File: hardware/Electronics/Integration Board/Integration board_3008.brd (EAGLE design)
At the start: 66.3 x 58.3 mm, 11 parts, among them J3 CONN_20X2

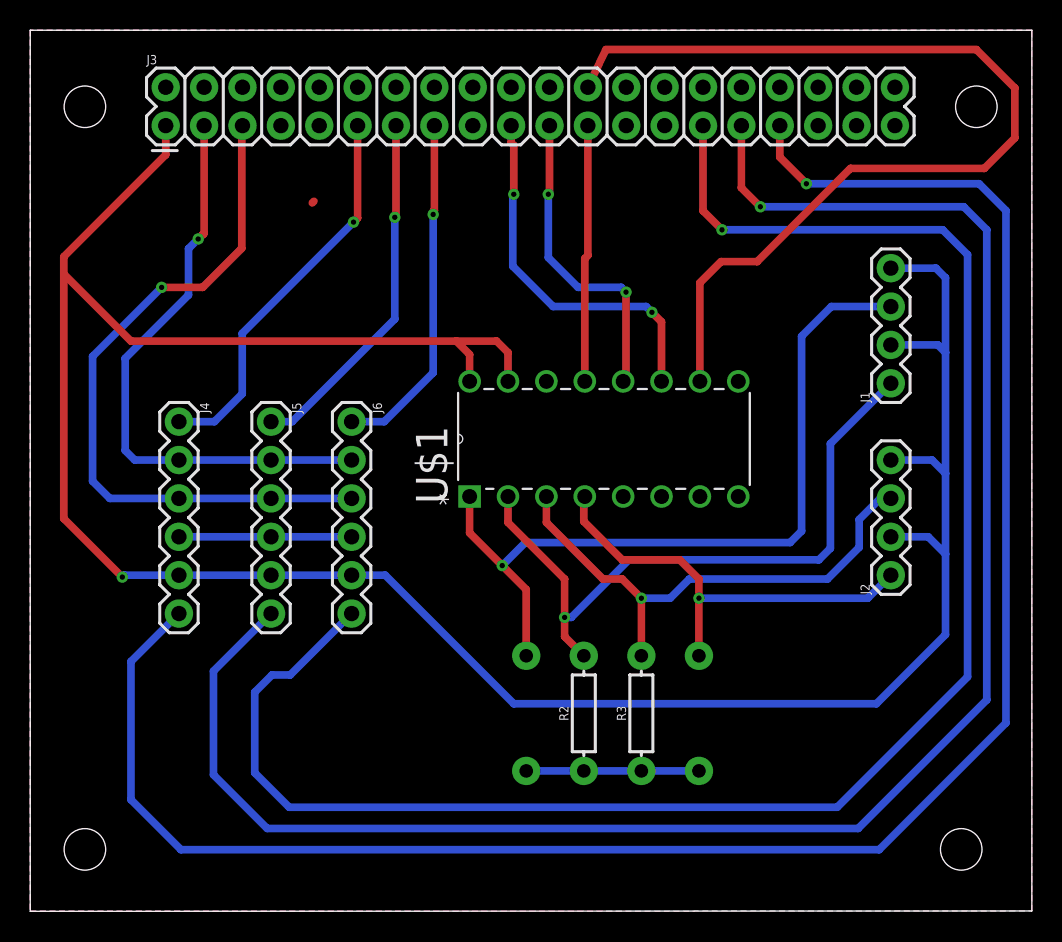
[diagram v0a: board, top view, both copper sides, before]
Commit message: Added IMU and Integration board schematic and layout PNG's
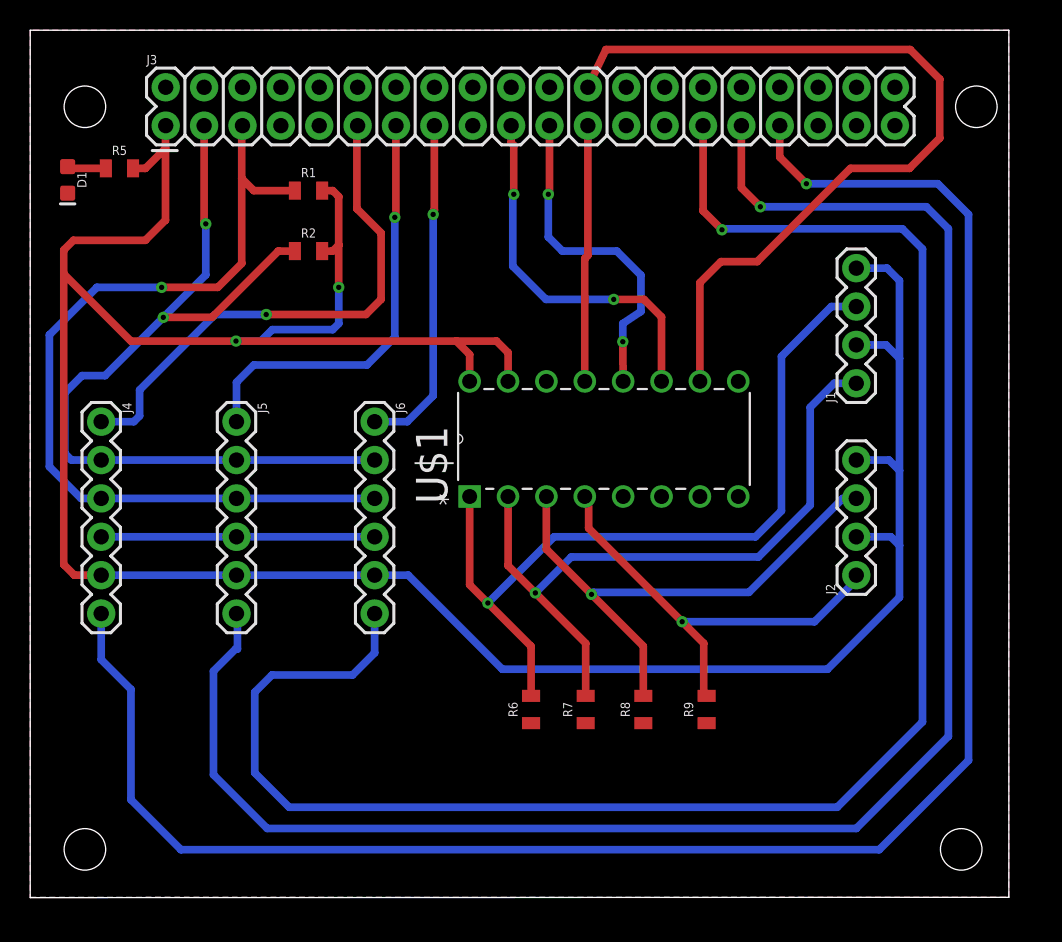
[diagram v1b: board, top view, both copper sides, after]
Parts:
- removed R3, R4: (no value), SparkFun-Resistors:AXIAL-0.3
- added D1: BLUE, SparkFun-LED:LED-0603
- added R5: 47ohm, SparkFun-Resistors:0805
- added R6, R7, R8, R9: 3.3k, SparkFun-Resistors:0805
- R1, R2: value (none) -> 10k; device SparkFun-Resistors:AXIAL-0.3 -> SparkFun-Resistors:0805
- moved R1 37.5 mm to (18.8, 41.2), flipped to the top, turned to 0 degrees
- moved R2 35.6 mm to (18.8, 37.2), turned to 0 degrees
- moved J4 5.14 mm to (5.08, 25.9)
- moved J1 2.29 mm to (55.1, 28.4)
- moved J2 2.29 mm to (55.1, 15.7)
- moved J5 2.29 mm to (14.0, 25.9)
- moved J6 1.52 mm to (23.2, 25.9)
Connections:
- new net N$11: D1.A, R5.1
- net GND: now also D1.C, R6.1, R7.1, R8.1, R9.1; no longer R1.P$1, R2.P$1, R3.P$1, R4.P$1
- net N$1: now also R6.2; no longer R1.P$2
- net N$15: now also R7.2; no longer R2.P$2
- net N$3: now also R8.2; no longer R3.P$2
- net N$4: now also R9.2; no longer R4.P$2
- net SCL: now also R1.1
- net SDA: now also R2.1
- net VCC: now also R1.2, R2.2, R5.2
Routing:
- net SDA: track 38.9 -> 57.7 mm, vias 1 -> 2
- net VCC: track 170.1 -> 185.8 mm, vias 1 -> 2
- net SCL: track 46.9 -> 58.8 mm
- net CS: track 65.5 -> 55.9 mm
- net N$2: track 25.9 -> 35.1 mm
- net GND: track 23.0 -> 18.1 mm
- net N$5: track 23.8 -> 28.4 mm
- net N$7: track 121.0 -> 116.6 mm
- net N$17: track 128.8 -> 124.7 mm
- net N$11: track 0.00 -> 2.58 mm
- net N$3: track 34.2 -> 36.0 mm
- net N$15: track 44.7 -> 46.1 mm
- net DOUT: track 20.8 -> 22.2 mm
- net N$1: track 52.5 -> 53.4 mm
- net N$6: track 117.9 -> 117.0 mm
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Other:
- board size 66.3 x 58.3 mm -> 64.8 x 57.4 mm
